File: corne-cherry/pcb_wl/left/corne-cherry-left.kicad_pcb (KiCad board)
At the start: 2 copper layers, 152.8 x 91.4 mm, 57 parts, among them J1 MJ-4PP-9, J2 OLED, J3 Conn_01x02_Female, SW1 SW_PUSH, SW10 SW_PUSH, SW11 SW_PUSH, SW12 SW_PUSH, SW13 SW_PUSH, SW14 SW_PUSH, SW15 SW_PUSH, SW16 SW_PUSH, SW17 SW_PUSH, SW18 SW_PUSH, SW19 SW_PUSH, SW2 SW_PUSH, SW20 SW_PUSH, SW21 SW_PUSH, SW22 SW_PUSH, SW23 SW_SPDT, SW3 SW_PUSH, SW4 SW_PUSH, SW5 SW_PUSH, SW6 SW_PUSH, SW7 SW_PUSH, SW8 SW_PUSH, SW9 SW_PUSH, U1 ProMicro

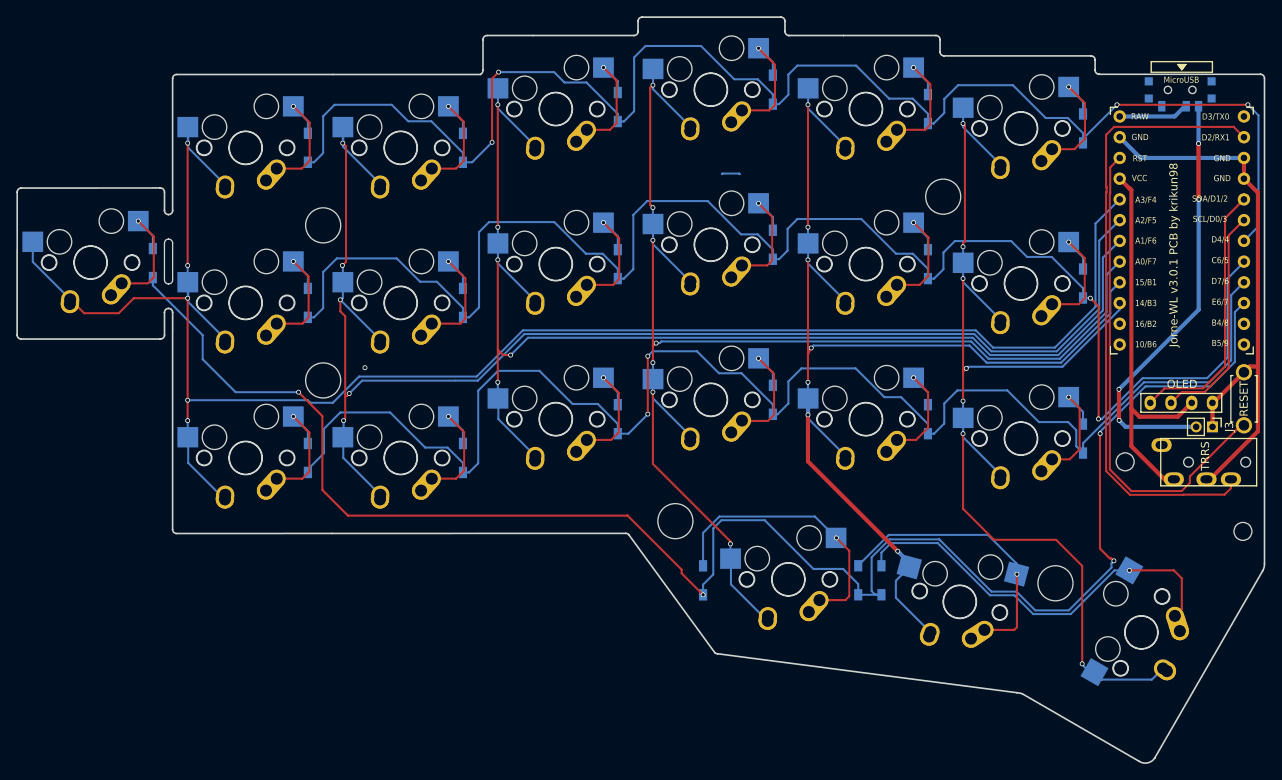
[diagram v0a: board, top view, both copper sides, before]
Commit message: Small revision bump: bigger battery header, smaller footprints
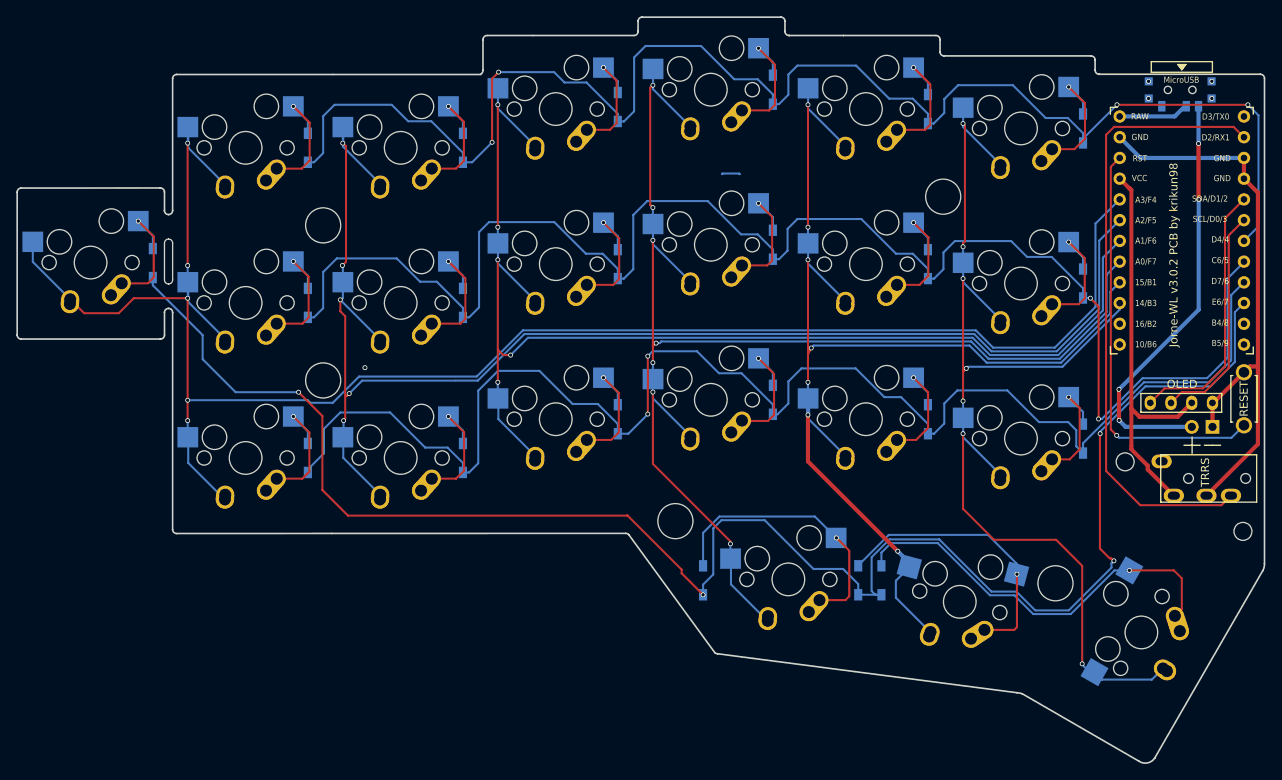
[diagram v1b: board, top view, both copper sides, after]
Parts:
- J3: footprint Connector_PinHeader_2.00mm:PinHeader_1x02_P2.00mm_Vertical -> kbd:Battery_Header
- moved J1 2.00 mm to (166.9, 71.4)
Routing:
- net reset: track 60.0 -> 51.4 mm, vias 0 -> 1
- net GND: track 69.6 -> 71.3 mm
- net VCC: track 49.2 -> 50.1 mm
- net (no net): vias 0 -> 4
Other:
- board text added: "Jorne-WL v3.0.2 PCB by krikun98"
- board text removed: "Jorne-WL v3.0.1 PCB by krikun98"
